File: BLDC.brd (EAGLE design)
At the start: 75.9 x 95.2 mm, 132 parts, among them U1 MCP2562, U2 STM32F405RGT6, U3 DRV8302, U4 LM3671MF-3.3/NOPB, Y1 8MHz

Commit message: changed via diameters
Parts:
- moved J2 54.7 mm to (35.2, 6.03)
- moved C15 28.5 mm to (47.6, 36.2), turned to 180 degrees
- moved C19 20.6 mm to (41.9, 25.1), turned to 180 degrees
- moved C13 19.9 mm to (41.9, 23.2), turned to 180 degrees
- moved C18 19.6 mm to (41.9, 21.3), turned to 180 degrees
- moved U2 12.6 mm to (51.4, 28.3), turned to 180 degrees
- moved C21 11.7 mm to (59.4, 27.9), turned to 270 degrees
- moved C23 10.4 mm to (36.5, 36.2), turned to 0 degrees
- moved C11 10.4 mm to (61.9, 16.5), turned to 270 degrees
- moved C25 10.1 mm to (36.5, 34.0), turned to 0 degrees
- moved C12 8.24 mm to (50.2, 18.7), turned to 180 degrees
- moved C10 7.96 mm to (61.0, 22.5), turned to 270 degrees
- moved C9 7.81 mm to (54.0, 25.7), turned to 90 degrees
- moved Y1 7.68 mm to (57.1, 25.7), turned to 180 degrees
- moved C27 5.43 mm to (36.5, 31.8), turned to 0 degrees
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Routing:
- net BR_SO1: track 1.05 -> 34.0 mm
- net BR_SO2: track 1.44 -> 34.0 mm
- net N$29: track 13.2 -> 4.33 mm, vias 2 -> 1
- net N$26: track 12.0 -> 5.10 mm, vias 2 -> 1
- net N$15: track 4.92 -> 11.7 mm
- net N$24: track 10.4 -> 4.28 mm, vias 2 -> 1
- net N$18: track 0.00 -> 6.11 mm
- net N$28: track 7.33 -> 3.04 mm, vias 2 -> 1
- net H2: track 7.34 -> 11.3 mm
- net GND: track 9.70 -> 13.1 mm, vias 0 -> 2
- net EN_GATE: track 7.95 -> 10.8 mm
- net H1: track 7.13 -> 9.99 mm
- net L1: track 7.38 -> 10.2 mm
- net L2: track 7.26 -> 10.1 mm
- net H3: track 7.24 -> 10.0 mm
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
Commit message: commited to micro JST connectors
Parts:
- removed J9: (no value), FormE:JST-1X4
- moved J8 276.8 mm to (107.0, 33.0)
- moved J1 275.3 mm to (96.5, 21.6)
- moved J7 209.5 mm to (52.1, 5.71)
- moved C11 29.7 mm to (65.4, 46.0), turned to 0 degrees
- moved C10 22.6 mm to (59.4, 45.1), turned to 180 degrees
- moved C20 20.8 mm to (60.3, 42.2), turned to 0 degrees
- moved C12 20.3 mm to (63.2, 34.3), turned to 270 degrees
- moved C17 19.7 mm to (61.6, 38.7), turned to 270 degrees
- moved C18 19.3 mm to (60.6, 26.0), turned to 270 degrees
- moved C13 17.1 mm to (58.7, 26.0), turned to 270 degrees
- moved C21 16.5 mm to (54.0, 43.5), turned to 0 degrees
- moved Y1 15.6 mm to (56.2, 41.3), turned to 90 degrees
- moved C19 15.0 mm to (56.8, 26.0), turned to 270 degrees
- moved C9 12.6 mm to (56.2, 38.1), turned to 0 degrees
- moved J6 11.0 mm to (104.1, 55.6), turned to 0 degrees
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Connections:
- net +5V: now also J1.P$7, J2.P$7; no longer J9.P$4
- net AUX_1: now also J1.P$6
- net AUX_2: now also J1.P$5
- net AUX_3: now also J1.P$4
- net AUX_4: now also J1.P$3
- net AUX_5: now also J1.P$2
- net AUX_6: now also J2.P$3
- net AUX_7: now also J2.P$2
- net AUX_8: now also J2.P$1
- net CAR_CAN_N: now also J2.P$5; no longer J9.P$2
- net CAR_CAN_P: now also J2.P$6; no longer J9.P$3
- net GND: now also J1.P$1, J2.P$4; no longer J9.P$1
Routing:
- net BR_SO2: track 34.0 -> 28.9 mm
- net BR_SO1: track 34.0 -> 29.6 mm

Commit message: figured out rough layout of connectors
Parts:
- moved J6 127.2 mm to (-22.9, 63.2), turned to 90 degrees
- moved C11 44.4 mm to (50.8, 4.13), turned to 270 degrees
- moved C12 36.9 mm to (39.1, 6.35), turned to 180 degrees
- moved C10 36.2 mm to (49.8, 10.2), turned to 270 degrees
- moved C17 35.7 mm to (43.5, 7.94), turned to 180 degrees
- moved C20 35.6 mm to (47.0, 9.21), turned to 270 degrees
- moved C18 34.4 mm to (30.8, 8.89), turned to 180 degrees
- moved JP1 32.4 mm to (-10.5, -2.22)
- moved R1 32.4 mm to (-10.5, 4.13)
- moved R2 32.4 mm to (-10.5, 7.94)
- moved R3 32.4 mm to (-14.3, 4.13)
- moved C13 31.8 mm to (30.8, 10.8), turned to 180 degrees
- moved Y1 29.7 mm to (46.0, 13.3), turned to 180 degrees
- moved C19 29.3 mm to (30.8, 12.7), turned to 180 degrees
- moved C21 28.5 mm to (48.3, 15.6), turned to 270 degrees
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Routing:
- net BR_SO1: track 29.6 -> 13.7 mm
- net BR_SO2: track 28.9 -> 13.7 mm
- net L3: track 1.53 -> 13.3 mm, vias 1 -> 0
- net H1: track 9.99 -> 18.3 mm, vias 2 -> 0
- net H3: track 10.0 -> 16.5 mm
- net H2: track 11.3 -> 17.1 mm
- net L1: track 10.2 -> 15.3 mm, vias 2 -> 0
- net +3V3: track 10.6 -> 15.2 mm, vias 1 -> 2
- net N$15: track 11.7 -> 15.2 mm
- net L2: track 10.1 -> 13.6 mm, vias 2 -> 0
- net HALL_3_OUT: track 2.82 -> 0.00 mm, vias 1 -> 0
- net USB_DM: track 1.11 -> 2.82 mm
- net AUX_4: track 0.00 -> 1.57 mm, vias 0 -> 1
- net GND: track 13.1 -> 12.0 mm
- net N$18: track 6.11 -> 5.27 mm
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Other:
- board size 75.9 x 95.2 mm -> 75.9 x 128.9 mm

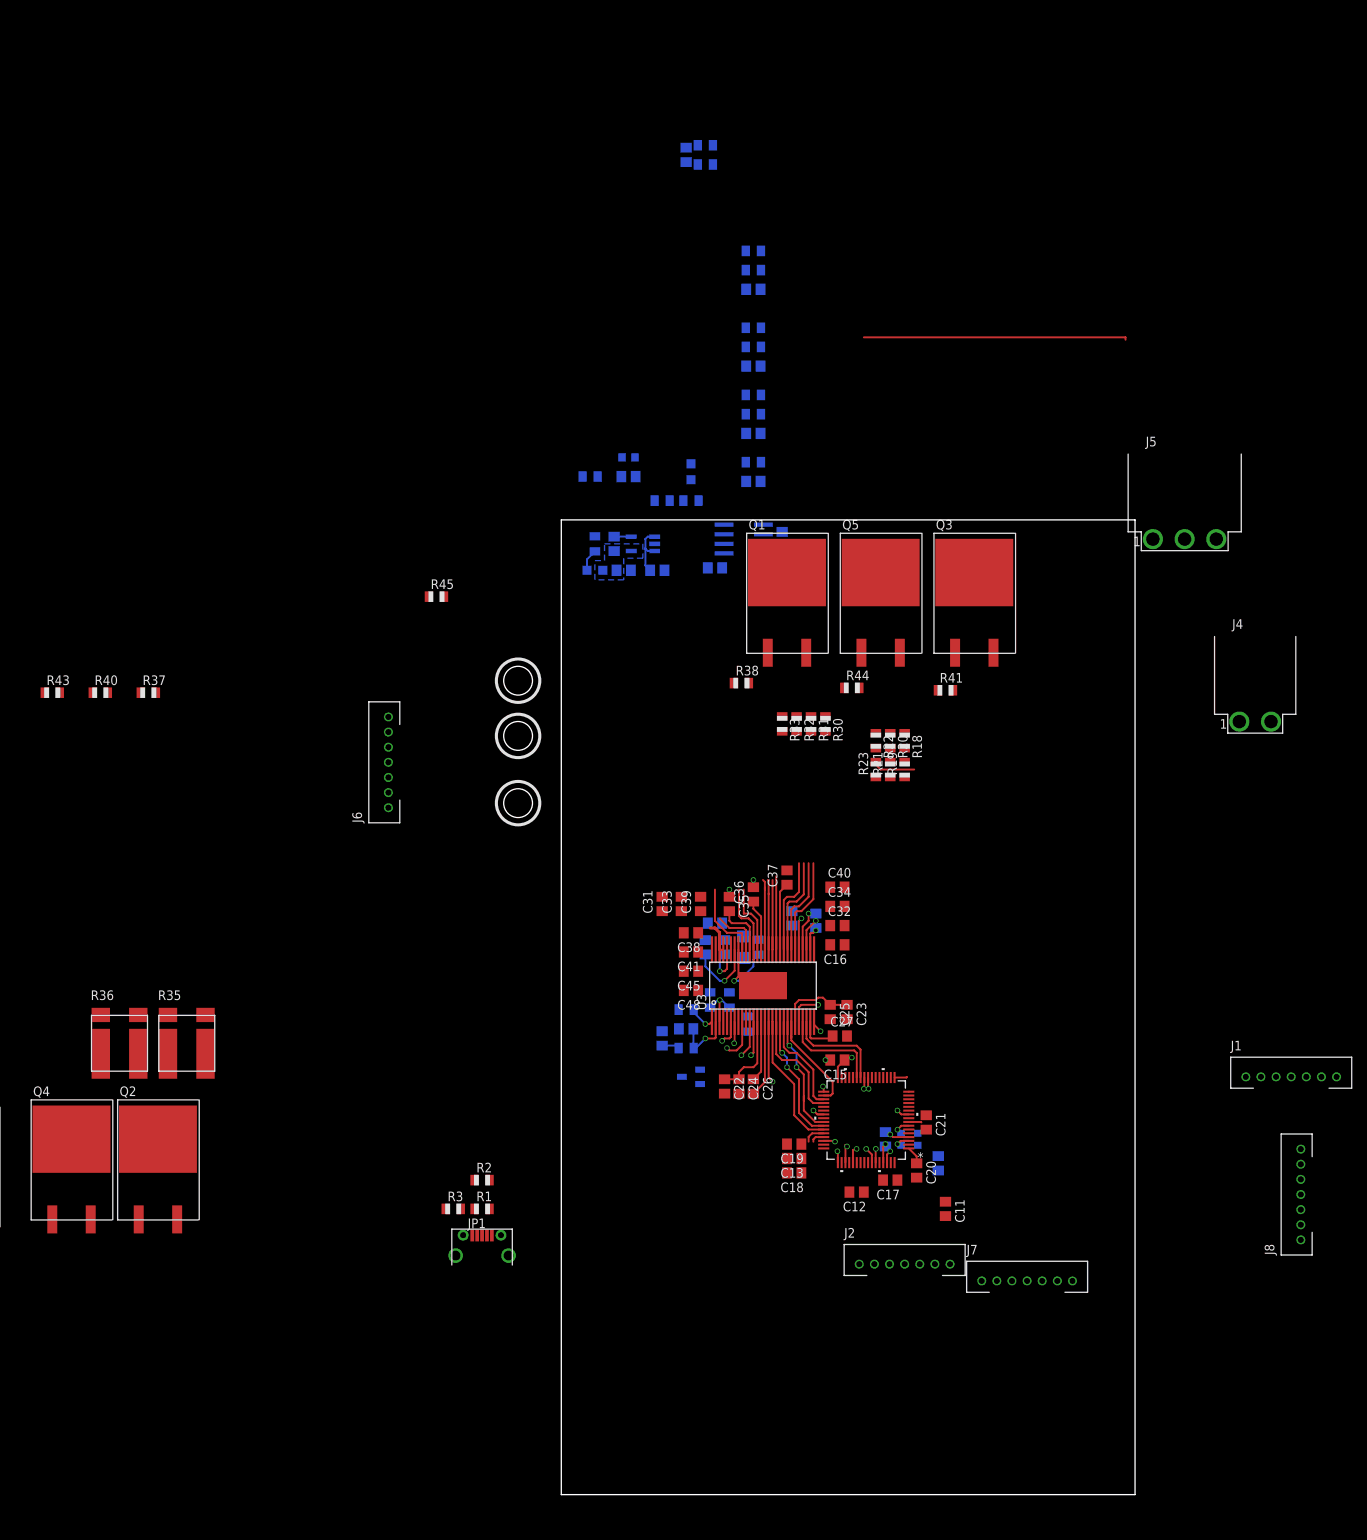
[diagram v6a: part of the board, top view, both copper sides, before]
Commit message: made very rough boarder dimentions and hole placement
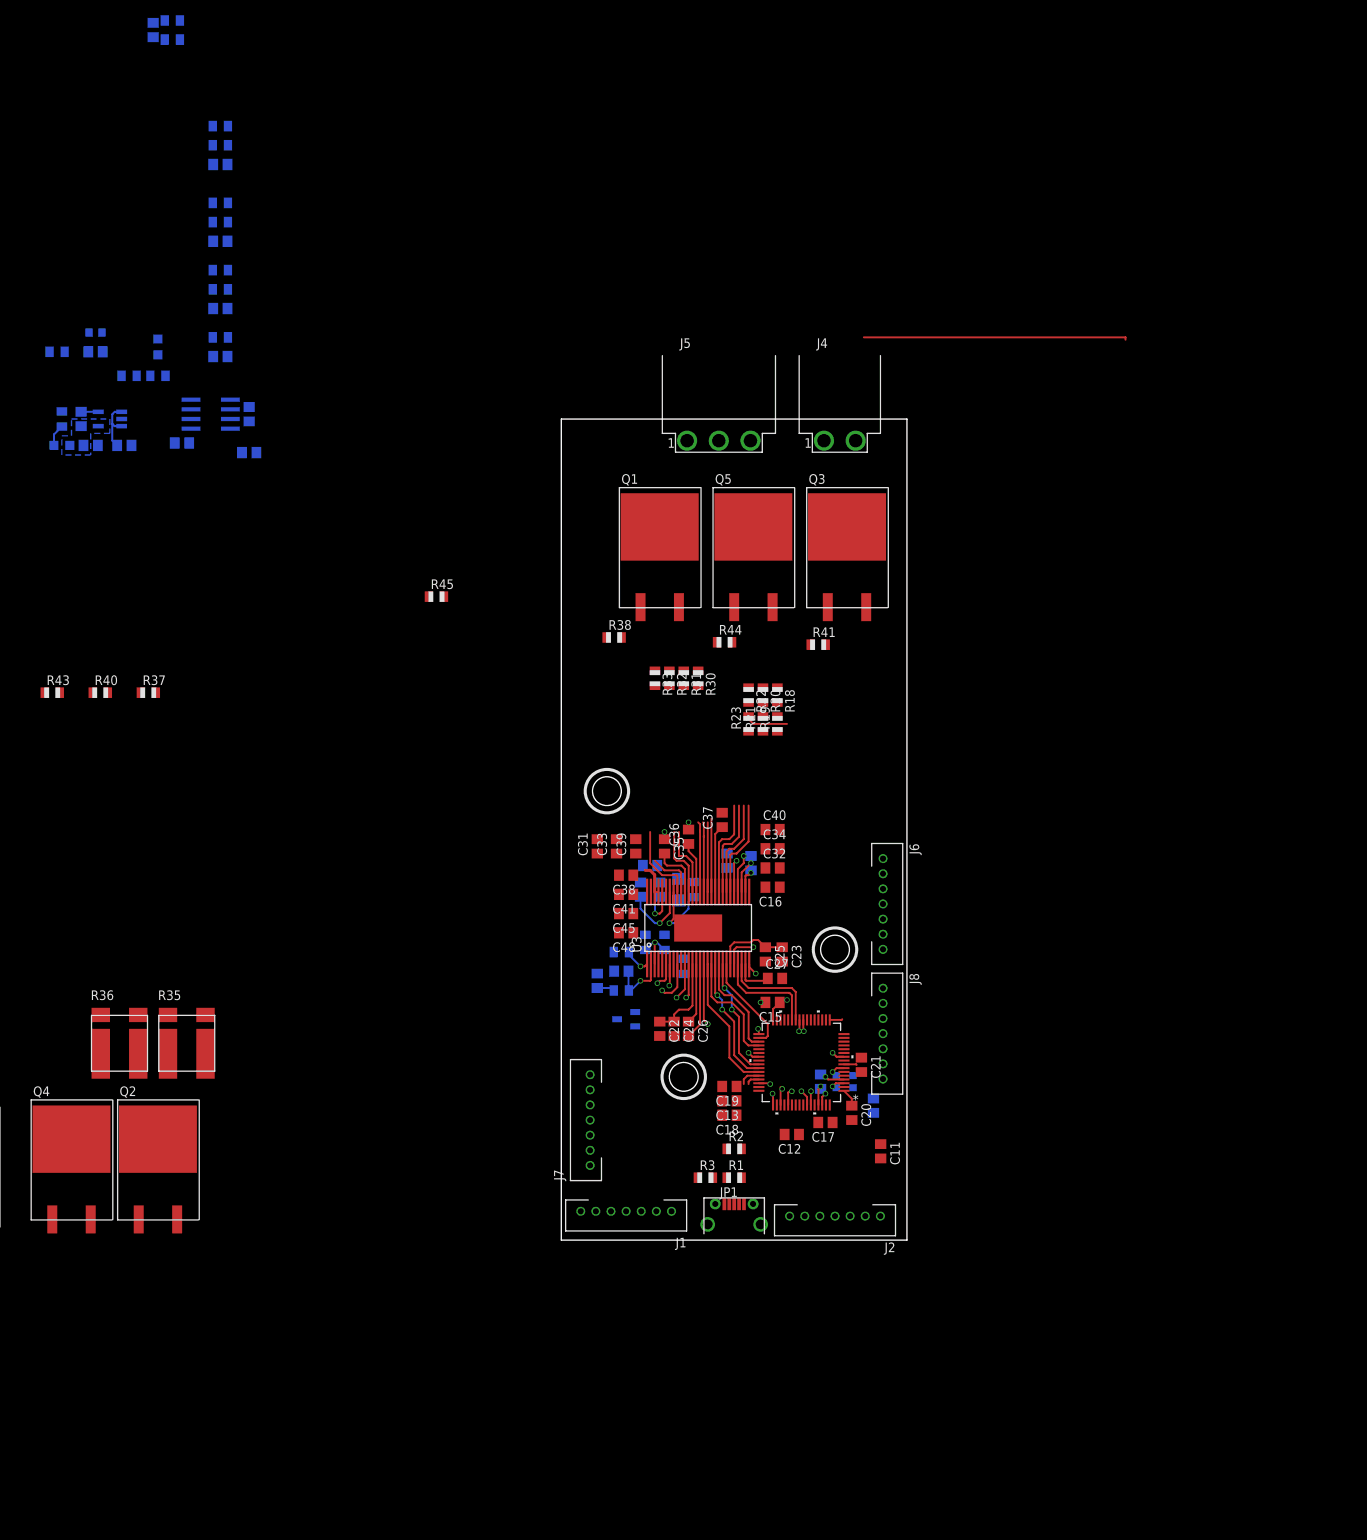
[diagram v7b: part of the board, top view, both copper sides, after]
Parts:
- moved J1 89.7 mm to (8.57, 3.81), turned to 180 degrees
- moved LED3 72.4 mm to (-66.0, 105.1)
- moved R34 72.4 mm to (-66.0, 108.6)
- moved C14 72.4 mm to (-61.6, 117.5)
- moved C2 72.4 mm to (-41.3, 104.1)
- moved C3 72.4 mm to (-45.1, 142.2)
- moved C30 72.4 mm to (-57.8, 105.1)
- moved C4 72.4 mm to (-45.1, 132.1)
- moved C46 72.4 mm to (-62.2, 105.1)
- moved C5 72.4 mm to (-45.1, 123.2)
- moved C6 72.4 mm to (-45.1, 116.8)
- moved C7 72.4 mm to (-50.2, 105.4)
- moved C8 72.4 mm to (-54.0, 160.0)
- moved L1 72.4 mm to (-63.5, 108.6)
- moved LED1 72.4 mm to (-53.3, 118.1)
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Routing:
- net H3: track 16.5 -> 15.9 mm
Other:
- board size 75.9 x 128.9 mm -> 45.7 x 108.6 mm

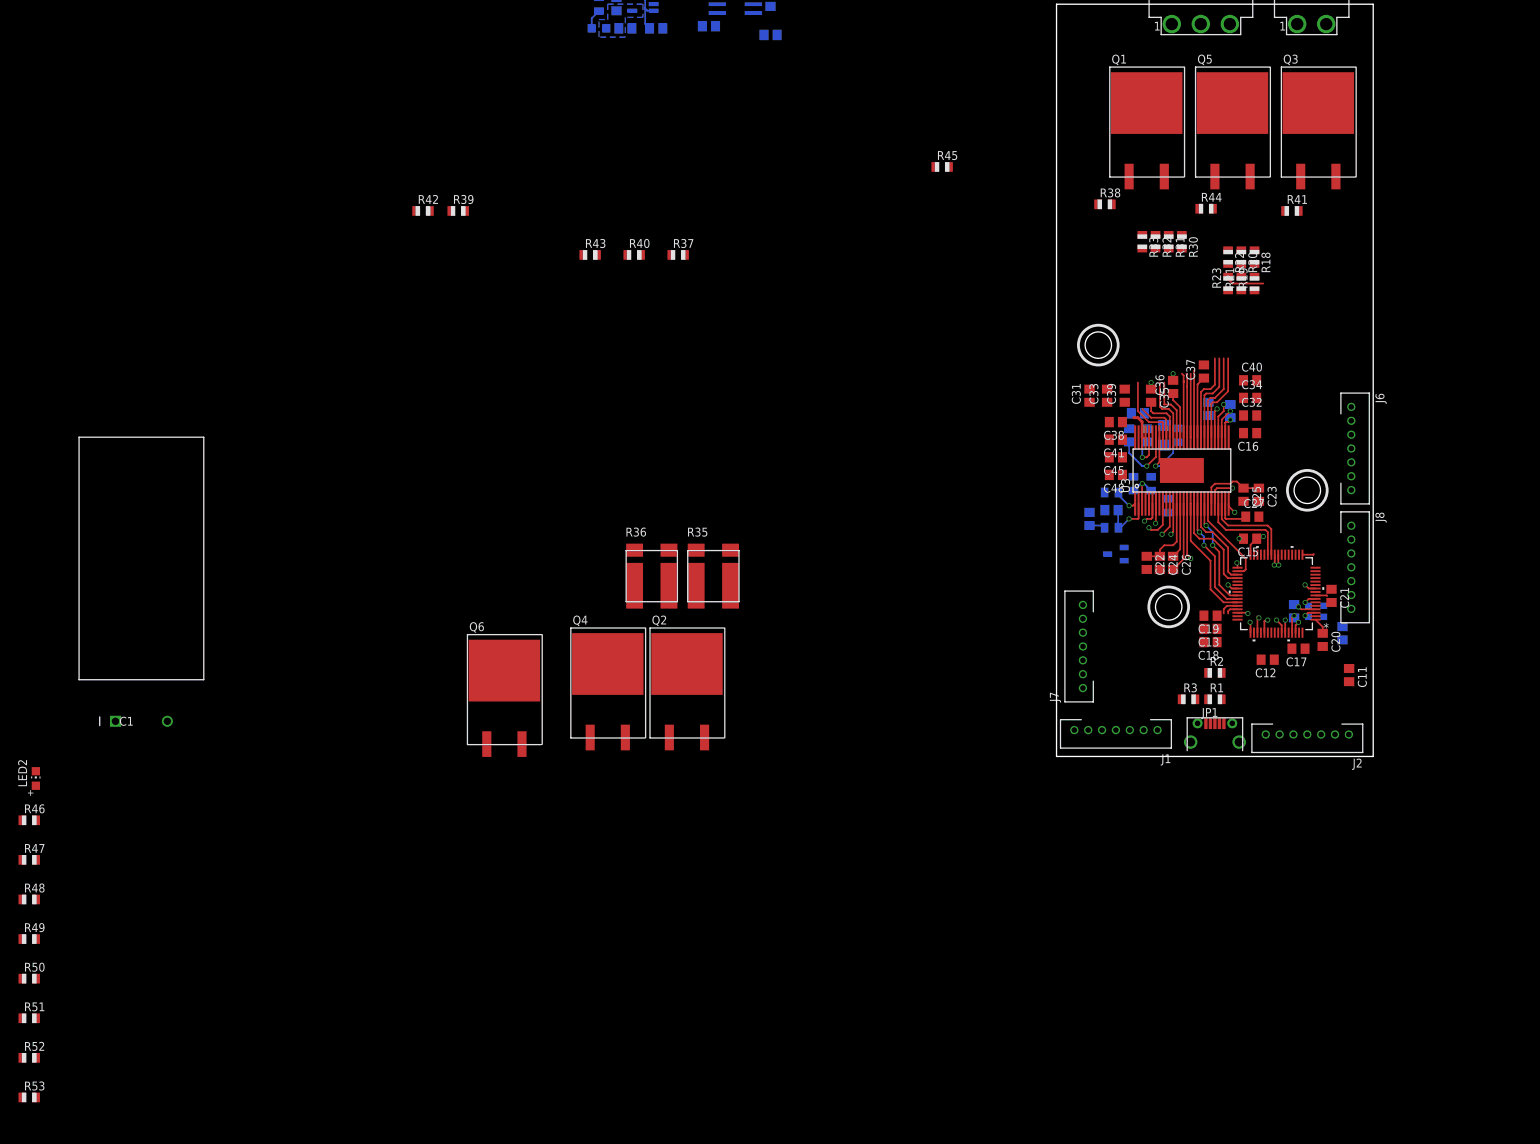
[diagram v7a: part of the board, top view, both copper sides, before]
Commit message: placed usb connect
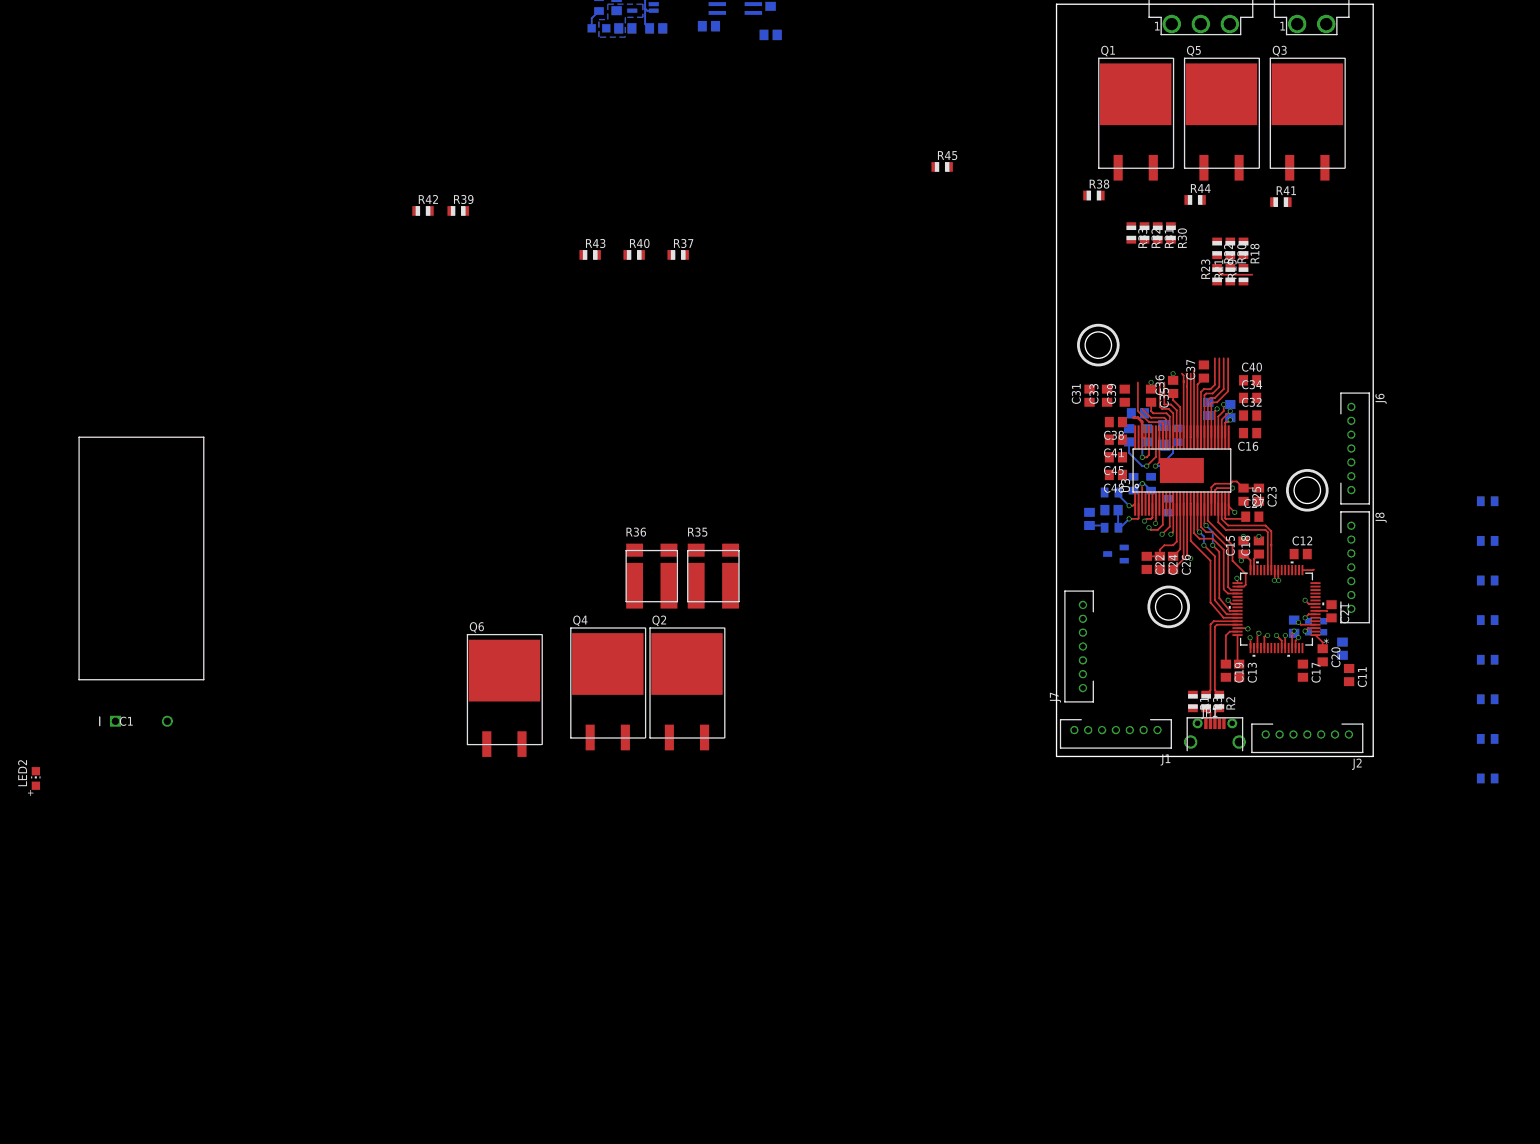
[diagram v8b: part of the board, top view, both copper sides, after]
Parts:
- moved R50 215.5 mm to (62.2, 14.0), flipped to the bottom
- moved R51 215.5 mm to (62.2, 8.26), flipped to the bottom
- moved R52 215.5 mm to (62.2, 2.54), flipped to the bottom
- moved R53 215.5 mm to (62.2, -3.17), flipped to the bottom
- moved R46 215.5 mm to (62.2, 36.8), flipped to the bottom
- moved R47 215.5 mm to (62.2, 31.1), flipped to the bottom
- moved R48 215.5 mm to (62.2, 25.4), flipped to the bottom
- moved R49 215.5 mm to (62.2, 19.7), flipped to the bottom
- moved C12 16.0 mm to (35.2, 29.2), turned to 0 degrees
- moved C18 15.3 mm to (29.2, 30.2), turned to 90 degrees
- moved C19 8.24 mm to (24.4, 12.4), turned to 270 degrees
- moved C13 7.31 mm to (26.4, 12.4), turned to 270 degrees
- moved R2 4.18 mm to (23.5, 7.94), turned to 270 degrees
- moved C17 3.24 mm to (35.6, 12.4), turned to 270 degrees
- moved R1 3.19 mm to (19.7, 7.94), turned to 270 degrees
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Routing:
- net USB_DP: track 1.80 -> 13.4 mm
- net USB_DM: track 2.82 -> 14.5 mm
- net N$6: track 0.00 -> 6.04 mm
- net +3V3: track 15.2 -> 20.6 mm, vias 2 -> 3
- net N$37: track 0.00 -> 2.61 mm
- net N$4: track 0.00 -> 2.44 mm
- net N$3: track 0.00 -> 2.44 mm
- net L1: track 15.3 -> 17.5 mm
- net L3: track 13.1 -> 15.3 mm
- net L2: track 13.6 -> 15.8 mm
- net BR_SO1: track 13.7 -> 15.9 mm
- net BR_SO2: track 13.7 -> 15.9 mm
- net H3: track 15.9 -> 18.0 mm
- net H2: track 17.1 -> 19.2 mm
- net H1: track 18.3 -> 20.4 mm
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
